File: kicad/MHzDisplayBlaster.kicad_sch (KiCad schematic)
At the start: 27 parts, among them J1 Conn_02x15 DigitLHS, J2 Conn_02x15 DigitRHS, J3 INPUT, J4 LED, J5 SW, Q1 2N7002, U1 DC56-11GWA, U2 74HCT04

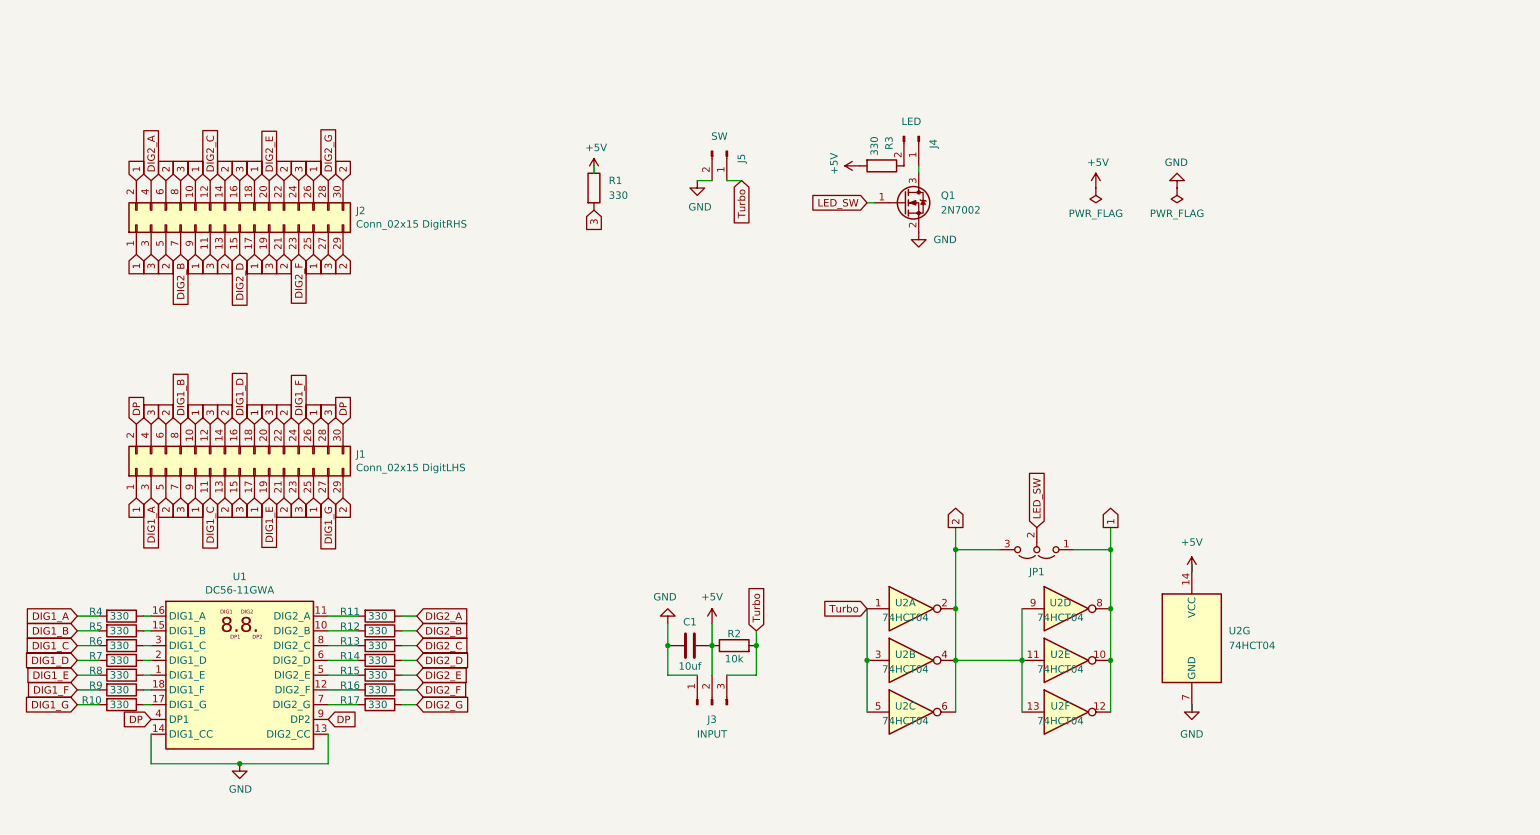
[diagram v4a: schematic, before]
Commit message: v1.3 - Anode resistors, mosfet power delivery, single channel inverter
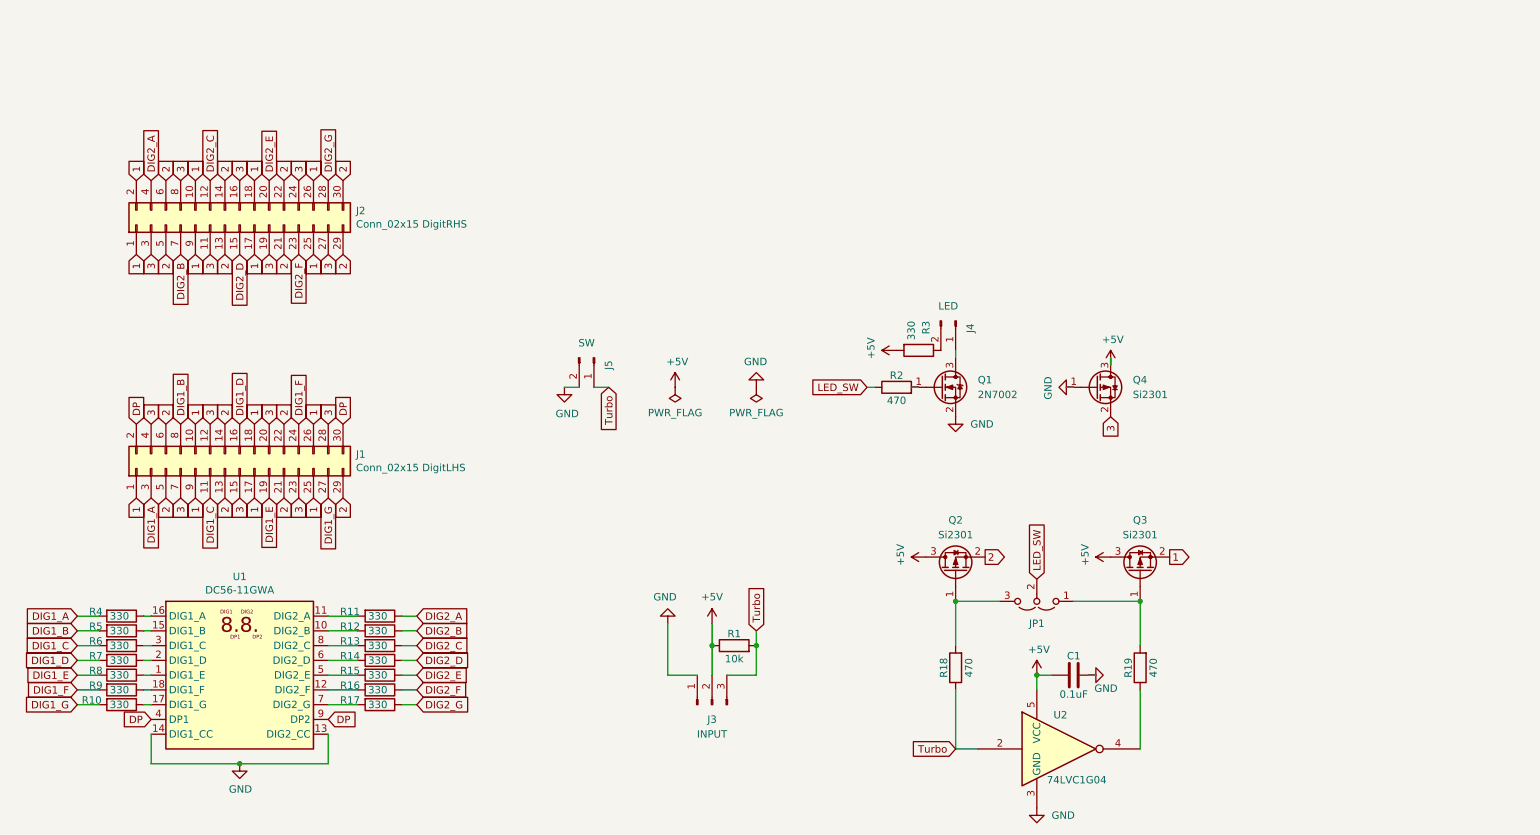
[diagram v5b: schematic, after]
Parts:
- removed R1: 330, Resistor_SMD:R_0805_2012Metric_Pad1.20x1.40mm_HandSolder, symbol Device:R
- removed U2: 74HCT04, Package_SO:SOIC-14_3.9x8.7mm_P1.27mm, symbol 74xx:74HCT04
- added Q2, Q3, Q4: Si2301, Package_TO_SOT_SMD:SOT-23-3, symbol Transistor_FET:Q_PMOS_GSD
- added R18, R19, R2: 470, Resistor_SMD:R_0805_2012Metric_Pad1.20x1.40mm_HandSolder, symbol Device:R
- added U2: 74LVC1G04, Package_TO_SOT_SMD:SOT-353_SC-70-5, symbol 74xGxx:74LVC1G04
- C1: value 10uf -> 0.1uF
- renumbered R2 to R1
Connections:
- net +5V: now also Q2.3 (D), Q3.3 (D), Q4.3 (D), U2.5 (VCC)
- net 1: now also Q3.2 (S); no longer JP1.1 (A)
- net 2: now also Q2.2 (S); no longer JP1.3 (B)
- net 3: now also Q4.2 (S)
- net GND: now also Q4.1 (G), U2.3 (GND)
- net LED_SW: now also R2.1; no longer Q1.1 (G)
- net Turbo: now also R18.1, U2.2
- new net: JP1.1 (A), Q3.1 (G), R19.2
- new net: JP1.3 (B), Q2.1 (G), R18.2
- new net: R19.1, U2.4
- new net: Q1.1 (G), R2.2
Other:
- moved on the sheet: J4, J5, JP1, Q1, R3

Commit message: v1.4 - Swap Si2301 pins for proper source and drain, fix 2N7002 gate
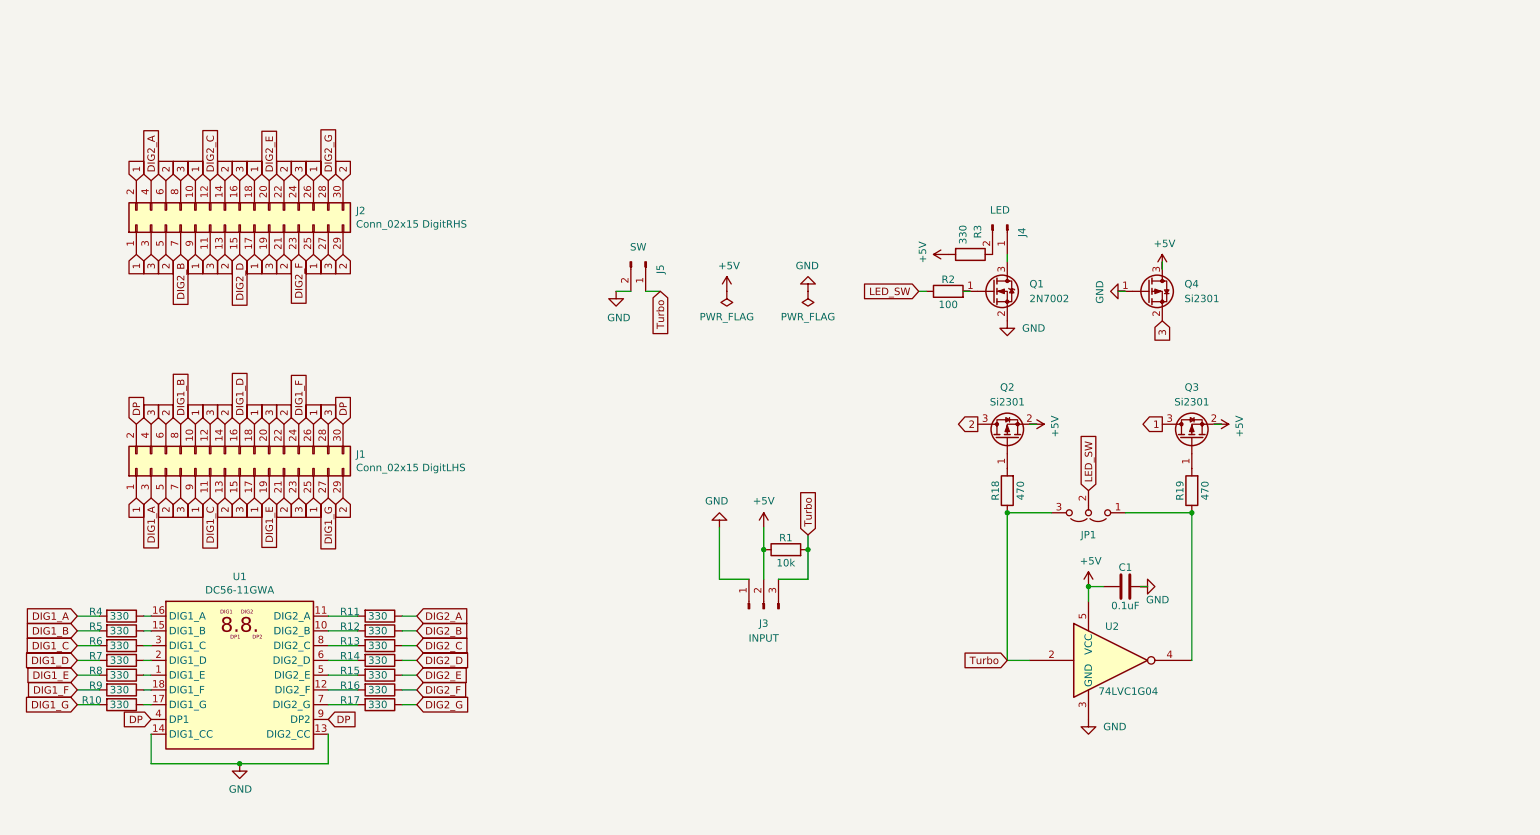
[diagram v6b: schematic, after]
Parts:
- R2: value 470 -> 100
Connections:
- net +5V: now also Q2.2 (S), Q3.2 (S); no longer Q2.3 (D), Q3.3 (D)
- net 1: now also Q3.3 (D); no longer Q3.2 (S)
- net 2: now also Q2.3 (D); no longer Q2.2 (S)
- net Turbo: now also JP1.3 (B)
- net at Q3.1 (G), R19.2: no longer JP1.1 (A)
- net at Q2.1 (G), R18.2: no longer JP1.3 (B)
- net at R19.1, U2.4: now also JP1.1 (A)
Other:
- company: Scrap Computing -> Innov8bit (Daniel Arnold)
- title: MHz Display Blaster -> ST-6A Blaster
- moved on the sheet: C1, J3, J4, J5, JP1, Q1, Q2, Q3, Q4, R1, R18, R19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
